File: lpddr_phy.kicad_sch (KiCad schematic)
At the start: 19 parts, among them U27 RK3576

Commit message: Add files via upload
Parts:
- removed C241, C247: 10u, Capacitor_SMD:C_0402_1005Metric, symbol New_Library_0:C_Small_edited
- removed C244: 100n, Capacitor_SMD:C_0201_0603Metric_Pad0.64x0.40mm_HandSolder, symbol New_Library_0:C_Small_edited
- removed C245, C246: 1u, Capacitor_SMD:C_0402_1005Metric, symbol New_Library_0:C_Small_edited
- removed C248, C249: 22u, Capacitor_SMD:C_0603_1608Metric, symbol New_Library_0:C_Small_edited
- added C123, C129, C130, C131: 22u, Capacitor_SMD:C_0603_1608Metric, symbol New_Library_0:C_Small_edited
- added C126: 1u, Capacitor_SMD:C_0201_0603Metric_Pad0.64x0.40mm_HandSolder, symbol New_Library_0:C_Small_edited
- added C127, C128: 1u, Capacitor_SMD:C_0402_1005Metric, symbol New_Library_0:C_Small_edited
- C120: renamed from C238; value 100n -> 1u
- renumbered C239 to C121, C240 to C122, C242 to C124, C243 to C125, C250 to C132, C251 to C133, C252 to C134, R115 to R36, R113 to R37, R114 to R38, U27 to U2
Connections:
- net GND: now also C123.2, C126.2, C127.2, C128.2, C129.2, C130.2, C131.2
- net VDDQ_DDR_S0: now also C123.1
- net VDD_DDR_S0: now also C126.1, C127.1, C128.1, C129.1, C130.1, C131.1
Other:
- moved on the sheet: C121, C122, C124, C125

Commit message: SBC Board V0.2
The SBC schematics before footprint and part number check
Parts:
- U3: renamed from U2; footprint (none) -> easyeda2kicad:FCCSP-698_L17.2-W16.1-TL_RK3576
- renumbered C120 to C128, C121 to C129, C122 to C130, C123 to C131, C124 to C132, C125 to C133, C126 to C134, C127 to C135, C128 to C136, C129 to C137, C130 to C138, C131 to C139, C132 to C140, C133 to C141, C134 to C142
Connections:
- no-connect marks 2 -> 4

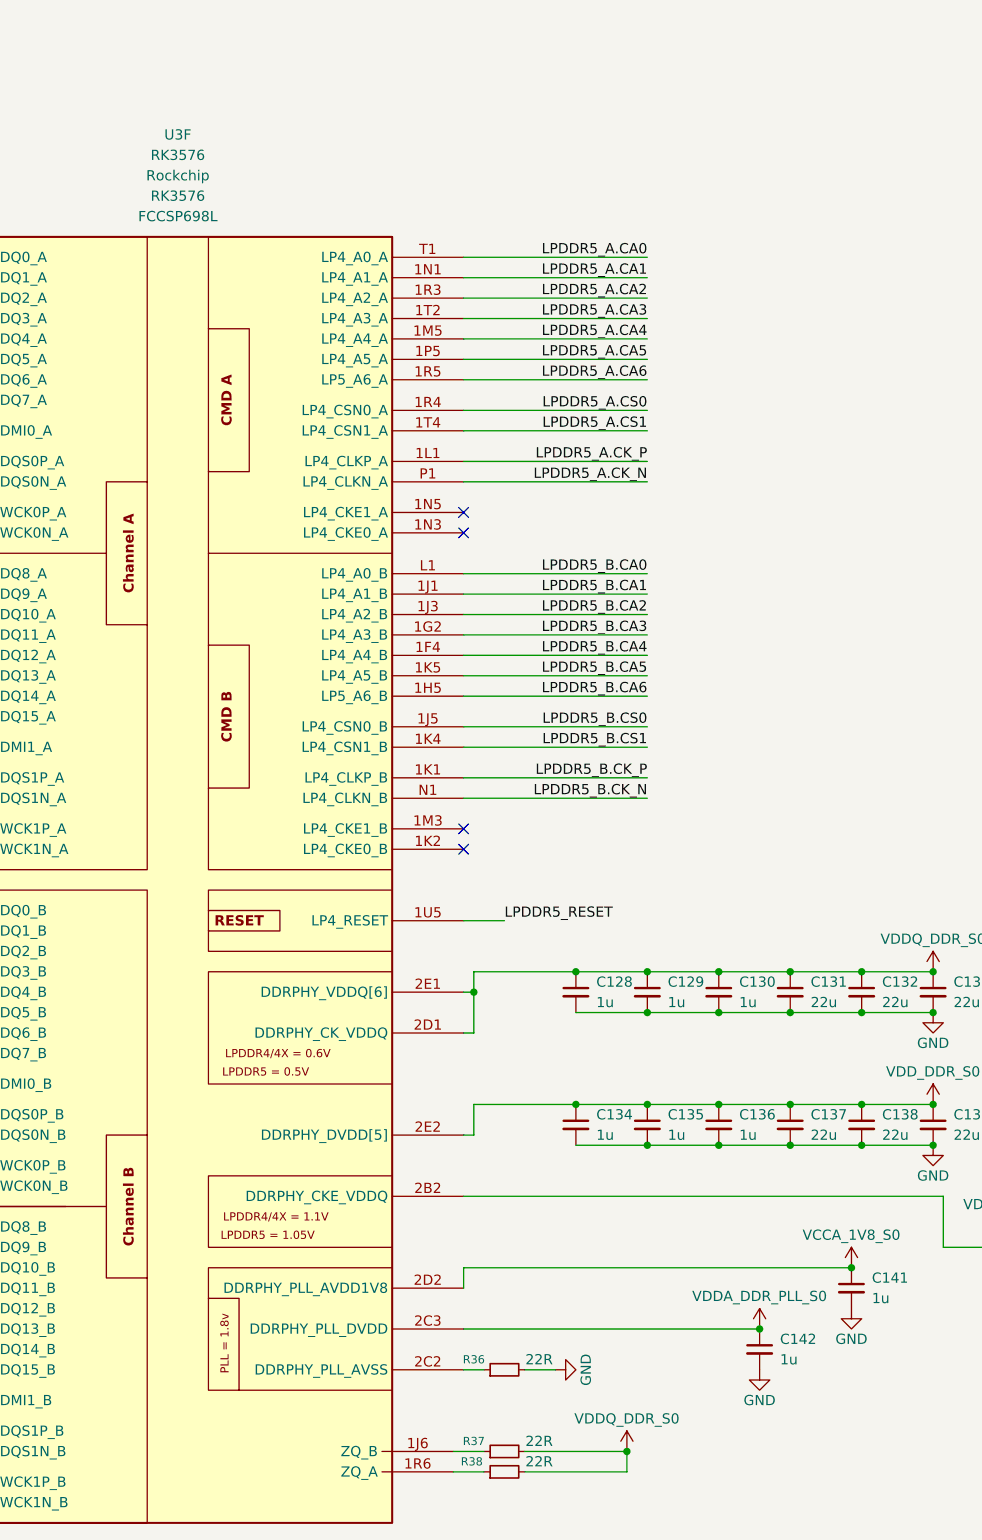
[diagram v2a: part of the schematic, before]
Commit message: SBCv0.3
there is no big thing update just some LCSC & Mouser parts
and Big problem deleted alot of component values (:
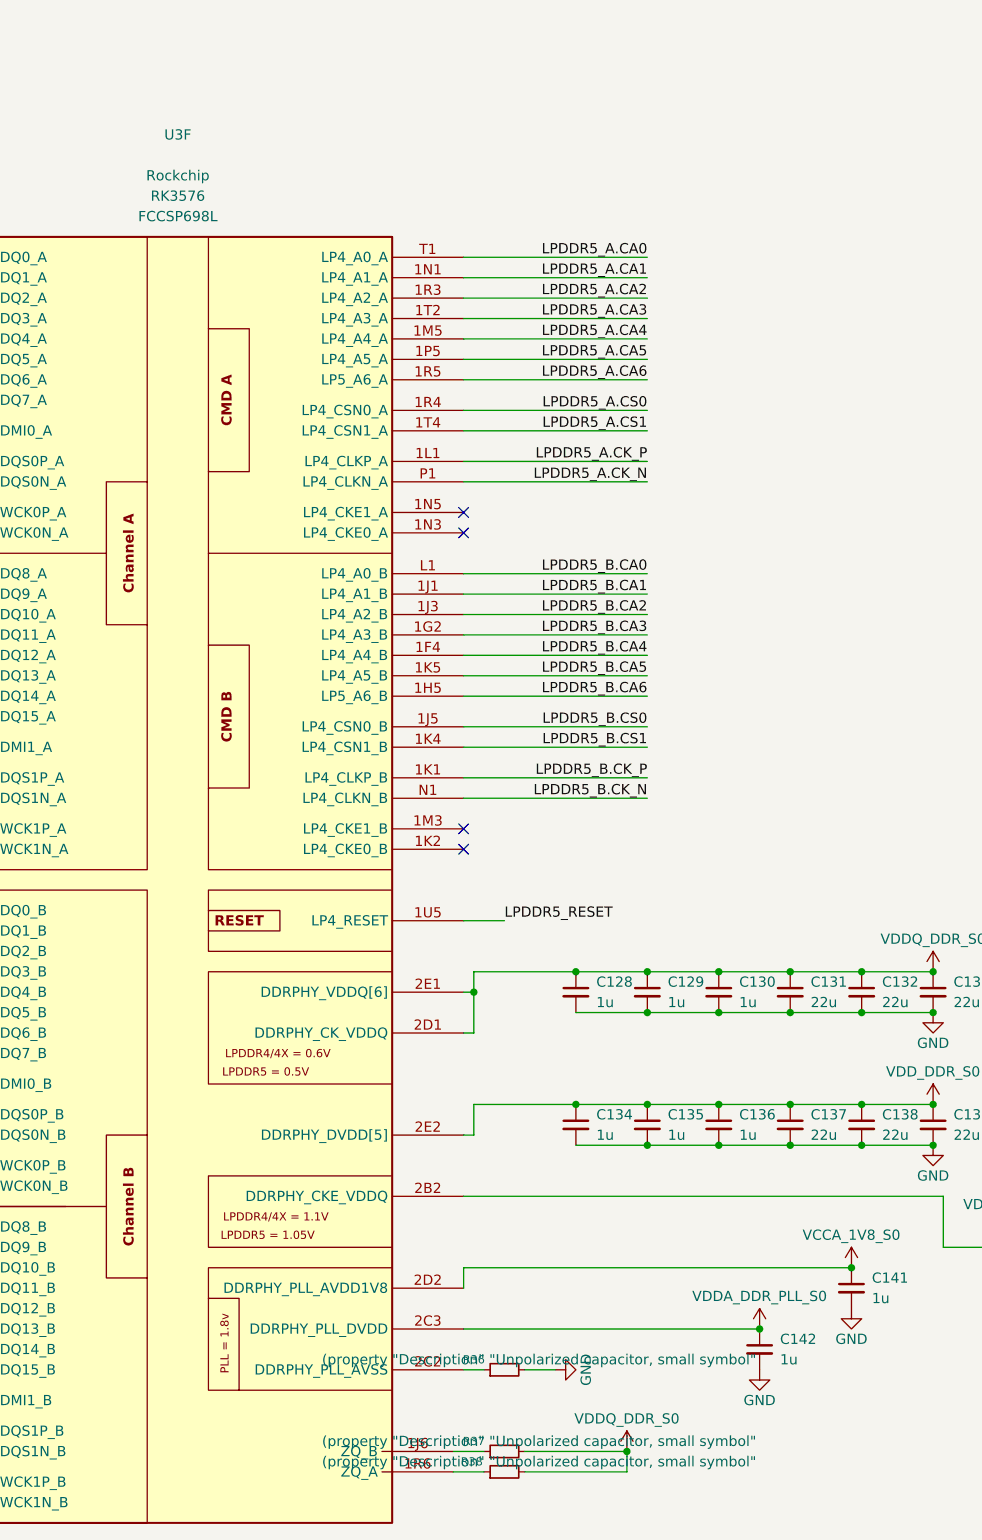
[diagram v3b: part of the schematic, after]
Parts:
- C128, C134: LCSC Part (none) -> C5209398; Mouser Part (none) -> CL03A105KP3NSNC
- C129, C130, C135, C136, C140, C141, C142: footprint Capacitor_SMD:C_0402_1005Metric -> Capacitor_SMD:C_0201_0603Metric_Pad0.64x0.40mm_HandSolder; LCSC Part (none) -> C5209398; Mouser Part (none) -> CL03A105KP3NSNC
- C131, C132, C133, C137, C138, C139: LCSC Part (none) -> C86295; Mouser Part (none) -> CL10A226MP8NUNE
- R36, R37, R38: value 22R -> (property "Description" "Unpolarized capacitor, small symbol"
- U3: value RK3576 -> (none); LCSC Part (none) -> (polyline

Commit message: SBCv0.4
add LCSC & Mouser parts 
and solve the deleted value in the past version
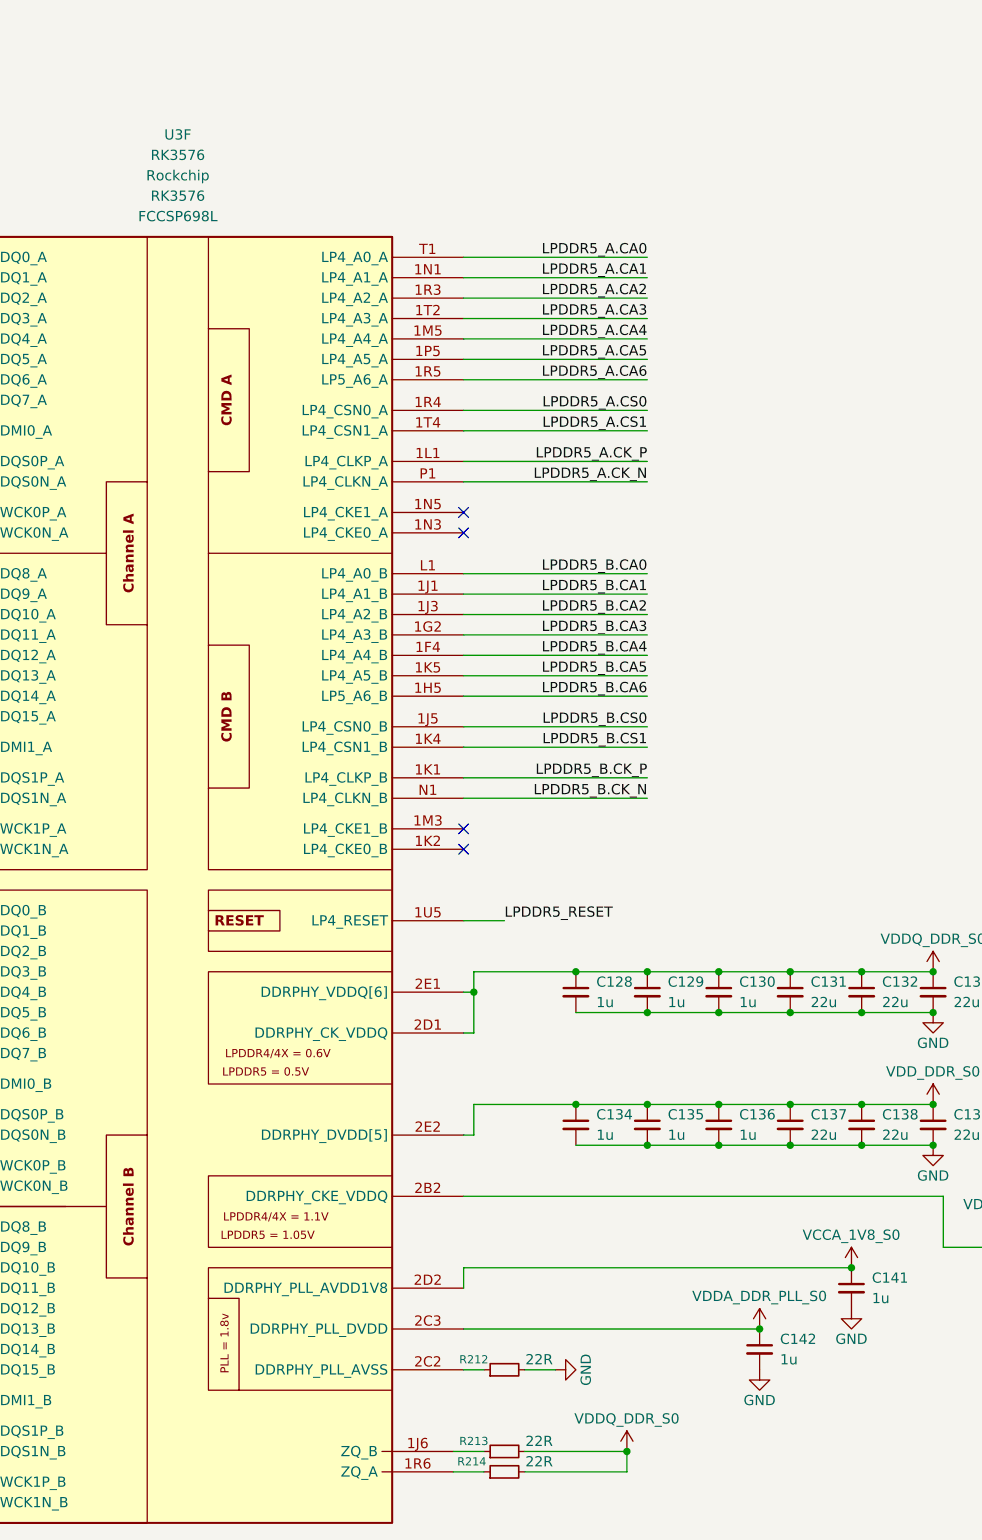
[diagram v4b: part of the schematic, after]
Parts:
- removed R36, R37, R38: (property "Description" "Unpolarized capacitor, s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, PCM_Resistor_SMD_AKL:R_0402_1005Metric_Pad0.72x0.64mm, symbol Device:R_Small
- added R212, R213, R214: 22R, PCM_Resistor_SMD_AKL:R_0402_1005Metric, symbol Device:R_Small
- U3: value (none) -> RK3576; LCSC Part (polyline -> C42388007
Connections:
- net GND: now also R212.2
- net VDDQ_DDR_S0: now also R213.2, R214.2
- net at U3.1J6 (ZQ_B): now also R213.1
- net at U3.1R6 (ZQ_A): now also R214.1
- net at U3.2C2 (DDRPHY_PLL_AVSS): now also R212.1
